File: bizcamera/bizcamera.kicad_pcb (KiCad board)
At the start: 4 copper layers, 84.5 x 55 mm, 81 parts, among them J1 Camera, J2 Micro_SD_Card_Det1, J3 USB_IN, SW1 USB_BOOT, SW3 Shutter, U1 RP2350_60QFN, U2 SPX3819M5-L-1-8, U3 S25FS128SDSNFI101, U4 ESP-PSRAM64, U5 SPX3819M5-L-3-3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

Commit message: Update bizcamera.kicad_pcb
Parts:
- moved R17 2.03 mm to (123.9, 67.9), turned to -90 degrees
- moved D1 1.89 mm to (125.5, 70.3)
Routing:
- net Net-(D1-A): track 74.2 -> 70.9 mm
- net /USB_DN: track 18.4 -> 19.4 mm
- net /USB_DP: track 20.2 -> 21.2 mm
- net -BATT: track 133.7 -> 133.5 mm, vias 23 -> 24
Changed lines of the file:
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@@
 	(footprint "LED_SMD:LED_1206_3216Metric_ReverseMount_Hole1.8x2.4mm"
 		(layer "F.Cu")
-		(at 125.42 68.46)
+		(at 125.46 70.35)
 		(descr "LED SMD 1206 (3216 Metric), reverse mount, square (rectangular) end terminal, IPC_7351 nominal, (Body size source: http://www.tortai-tech.com/upload/download/2011102023233369053.pdf), generated with kicad-footprint-generator")
 		(tags "diode reverse")
@@
 	(footprint "Resistor_SMD:R_0402_1005Metric"
 		(layer "F.Cu")
-		(at 123.45 65.91)
+		(at 123.92 67.88 -90)
 		(descr "Resistor SMD 0402 (1005 Metric), square (rectangular) end terminal, IPC_7351 nominal, (Body size source: IPC-SM-782 page 72, https://www.pcb-3d.com/wordpress/wp-content/uploads/ipc-sm-782a_amendment_1_and_2.pdf), generated with kicad-footprint-generator")
 		(tags "resistor")
 		(property "Reference" "R17"
-			(at 0 -1.17 0)
+			(at 0 -1.17 90)
 			(layer "F.SilkS")
 			(hide yes)
@@
 		)
 		(property "Value" "1k"
-			(at 0 1.17 0)
+			(at 0 1.17 90)
 			(layer "F.Fab")
 			(effects
@@
 		)
 		(property "Footprint" "Resistor_SMD:R_0402_1005Metric"
-			(at 0 0 0)
+			(at 0 0 -90)
 			(unlocked yes)
 			(layer "F.Fab")
@@
 		)
 		(property "Datasheet" ""
-			(at 0 0 0)
+			(at 0 0 -90)
 			(unlocked yes)
 			(layer "F.Fab")
@@
 		)
 		(property "Description" "Resistor"
-			(at 0 0 0)
+			(at 0 0 -90)
 			(unlocked yes)
 			(layer "F.Fab")
@@
 		(attr smd)
 		(fp_line
-			(start -0.153641 -0.38)
-			(end 0.153641 -0.38)
+			(start -0.153641 0.38)
+			(end 0.153641 0.38)
 			(stroke
 				(width 0.12)
@@
 		)
 		(fp_line
-			(start -0.153641 0.38)
-			(end 0.153641 0.38)
+			(start -0.153641 -0.38)
+			(end 0.153641 -0.38)
 			(stroke
 				(width 0.12)
@@
 		)
 		(fp_line
-			(start -0.93 -0.47)
-			(end 0.93 -0.47)
+			(start -0.93 0.47)
+			(end -0.93 -0.47)
 			(stroke
 				(width 0.05)
@@
 		)
 		(fp_line
-			(start -0.93 0.47)
-			(end -0.93 -0.47)
+			(start 0.93 0.47)
+			(end -0.93 0.47)
 			(stroke
 				(width 0.05)
@@
 		)
 		(fp_line
-			(start 0.93 -0.47)
-			(end 0.93 0.47)
+			(start -0.93 -0.47)
+			(end 0.93 -0.47)
 			(stroke
 				(width 0.05)
@@
 		)
 		(fp_line
-			(start 0.93 0.47)
-			(end -0.93 0.47)
+			(start 0.93 -0.47)
+			(end 0.93 0.47)
 			(stroke
 				(width 0.05)
@@
 		)
 		(fp_line
-			(start -0.525 -0.27)
-			(end 0.525 -0.27)
+			(start -0.525 0.27)
+			(end -0.525 -0.27)
 			(stroke
 				(width 0.1)
@@
 		)
 		(fp_line
-			(start -0.525 0.27)
-			(end -0.525 -0.27)
+			(start 0.525 0.27)
+			(end -0.525 0.27)
 			(stroke
 				(width 0.1)
@@
 		)
 		(fp_line
-			(start 0.525 -0.27)
-			(end 0.525 0.27)
+			(start -0.525 -0.27)
+			(end 0.525 -0.27)
 			(stroke
 				(width 0.1)
@@
 		)
 		(fp_line
-			(start 0.525 0.27)
-			(end -0.525 0.27)
+			(start 0.525 -0.27)
+			(end 0.525 0.27)
 			(stroke
 				(width 0.1)
@@
 		)
 		(fp_text user "${REFERENCE}"
-			(at 0 0 0)
+			(at 0 0 90)
 			(layer "F.Fab")
 			(effects
@@
 		)
 		(pad "1" smd roundrect
-			(at -0.51 0)
+			(at -0.51 0 270)
 			(size 0.54 0.64)
 			(layers "F.Cu" "F.Paste" "F.Mask")
@@
 		)
 		(pad "2" smd roundrect
-			(at 0.51 0)
+			(at 0.51 0 270)
 			(size 0.54 0.64)
 			(layers "F.Cu" "F.Paste" "F.Mask")
@@
 	)
 	(segment
-		(start 121.915 66.935)
-		(end 121.915 67.98)
-		(width 0.35)
-		(layer "F.Cu")
-		(net 2)
-	)
-	(segment
 		(start 177.857501 114.8925)
 		(end 176.6475 113.682499)
@@
 	)
 	(segment
+		(start 122.525 67.37)
+		(end 121.915 67.98)
+		(width 0.35)
+		(layer "F.Cu")
+		(net 2)
+	)
+	(segment
 		(start 181.050768 93.82)
 		(end 180.02625 93.82)
@@
 	)
 	(segment
-		(start 122.94 65.91)
-		(end 121.915 66.935)
-		(width 0.35)
-		(layer "F.Cu")
-		(net 2)
-	)
-	(segment
 		(start 112.49 92.25)
 		(end 116.78 92.25)
@@
 	)
 	(segment
+		(start 123.92 67.37)
+		(end 122.525 67.37)
+		(width 0.35)
+		(layer "F.Cu")
+		(net 2)
+	)
+	(segment
 		(start 187.72 85.68)
 		(end 187.69 85.65)
@@
 	)
 	(via
+		(at 148.19 113.7)
+		(size 0.5)
+		(drill 0.3)
+		(layers "F.Cu" "B.Cu")
+		(net 2)
+	)
+	(via
 		(at 172.3 107)
 		(size 0.6)
@@
 	)
 	(segment
-		(start 123.96 65.91)
-		(end 123.96 68.37)
+		(start 123.96 70.3)
+		(end 123.91 70.35)
 		(width 0.5)
 		(layer "F.Cu")
@@
 	)
 	(segment
+		(start 123.92 70.34)
+		(end 123.91 70.35)
+		(width 0.35)
+		(layer "F.Cu")
+		(net 47)
+	)
+	(segment
+		(start 123.92 68.39)
+		(end 123.92 70.34)
+		(width 0.35)
+		(layer "F.Cu")
+		(net 47)
+	)
+	(segment
 		(start 152.35 110.2)
 		(end 152.35 109.44)
@@
 	)
 	(segment
+		(start 178.9275 97.5325)
+		(end 178.9275 96.5125)
+		(width 0.2)
+		(layer "F.Cu")
+		(net 50)
+	)
+	(segment
 		(start 187.279999 89.25)
 		(end 188.255 89.25)
@@
 	)
 	(segment
-		(start 126.97 68.46)
-		(end 126.97 67.47)
-		(width 0.35)
-		(layer "F.Cu")
-		(net 64)
-	)
-	(segment
-		(start 126.97 67.47)
-		(end 126.6 67.1)
-		(width 0.35)
-		(layer "F.Cu")
-		(net 64)
-	)
-	(segment
 		(start 183.0975 105.5425)
 		(end 182.48624 105.5425)
@@
 	)
 	(via
-		(at 126.6 67.1)
+		(at 127.01 70.35)
 		(size 0.7)
 		(drill 0.4)
@@
 	)
 	(segment
-		(start 126.6 67.1)
-		(end 129.18 69.68)
-		(width 0.5)
-		(layer "In2.Cu")
-		(net 64)
-	)
-	(segment
-		(start 136.71206 69.68)
+		(start 137.38206 70.35)
 		(end 172.46206 105.43)
 		(width 0.5)
@@
 	)
 	(segment
-		(start 129.18 69.68)
-		(end 136.71206 69.68)
-		(width 0.5)
-		(layer "In2.Cu")
-		(net 64)
-	)
-	(segment
 		(start 182.19285 105.83589)
 		(end 181.78696 105.43)
@@
 	)
 	(segment
+		(start 127.01 70.35)
+		(end 137.38206 70.35)
+		(width 0.5)
+		(layer "In2.Cu")
+		(net 64)
+	)
+	(segment
 		(start 181.66 108.18)
 		(end 181.66 109.02)
@@
 		(width 0.2)
 		(layer "F.Cu")
+		(net 67)
+	)
+	(segment
+		(start 179.9175 97.5425)
+		(end 179.9175 96.5225)
+		(width 0.2)
+		(layer "F.Cu")

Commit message: Styling
Styling to make it more of a business card :D
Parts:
- removed kibuzzard-6824811E: G***, kibuzzard-6824811E
- removed kibuzzard-68248180: G***, kibuzzard-68248180
- added G***: LOGO, Kiyo:Blahaj Exposed copper, F.Cu at (134.3, 69.2)
- added REF**: KiCad-Logo2_5mm_Copper-exposed, Kiyo:KiCad-Logo2_5mm_Copper-exposed, F.Cu at (142.5, 72.4)
- added kibuzzard-68265B48: G***, kibuzzard-68265B48, B.Cu at (173.7, 72.0)
- added kibuzzard-68265CCE: G***, kibuzzard-68265CCE, B.Cu at (137.6, 72.5)
- added kibuzzard-68265CF0: G***, kibuzzard-68265CF0, B.Cu at (119.8, 70.3)
- added kibuzzard-68265EBA: G***, kibuzzard-68265EBA, F.Cu at (190.8, 103.6)
- added kibuzzard-68265EEF: G***, kibuzzard-68265EEF, F.Cu at (170.7, 77.1)
- added kibuzzard-68265F1C: G***, kibuzzard-68265F1C, F.Cu at (177.1, 76.6)
- added kibuzzard-68265F3A: G***, kibuzzard-68265F3A, F.Cu at (193.3, 98.4)
- added kibuzzard-68265F49: G***, kibuzzard-68265F49, F.Cu at (153.6, 93.0)
- added kibuzzard-68265FA3: G***, kibuzzard-68265FA3, F.Cu at (134.0, 113.4)
- added kibuzzard-68265FBA: G***, kibuzzard-68265FBA, F.Cu at (185.1, 85.2)
- added kibuzzard-68265FD3: G***, kibuzzard-68265FD3, F.Cu at (185.0, 89.0)
- added kibuzzard-68265FDC: G***, kibuzzard-68265FDC, F.Cu at (119.5, 113.4)
- added kibuzzard-68266036: G***, kibuzzard-68266036, F.Cu at (169.8, 106.7)
- moved C22 1.12 mm to (183.0, 87.3), turned to 90 degrees
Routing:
- net +5V: track 28.7 -> 21.6 mm
- net +3V3: track 34.9 -> 32.4 mm, vias 13 -> 12
- net /QSPI_SS: track 4.40 -> 6.17 mm
- net /SCLK: track 37.4 -> 39.2 mm
- net /SPI_DO: track 35.6 -> 37.4 mm
- net /SPI_CS: track 40.0 -> 41.7 mm
- net /SD_DET: track 36.7 -> 38.4 mm
- net /SPI_DI: track 39.5 -> 41.0 mm
- net +1V8: track 244.6 -> 243.4 mm, vias 11 -> 12
- net -BATT: track 133.5 -> 133.8 mm, vias 24 -> 27
- added copper zone on F.Cu, net +5V
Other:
- board text added: "Liam Brooks Photographer Hobby PCB Designer https://kiyoo.moe github: korewakiyo discord: korewakiyo"

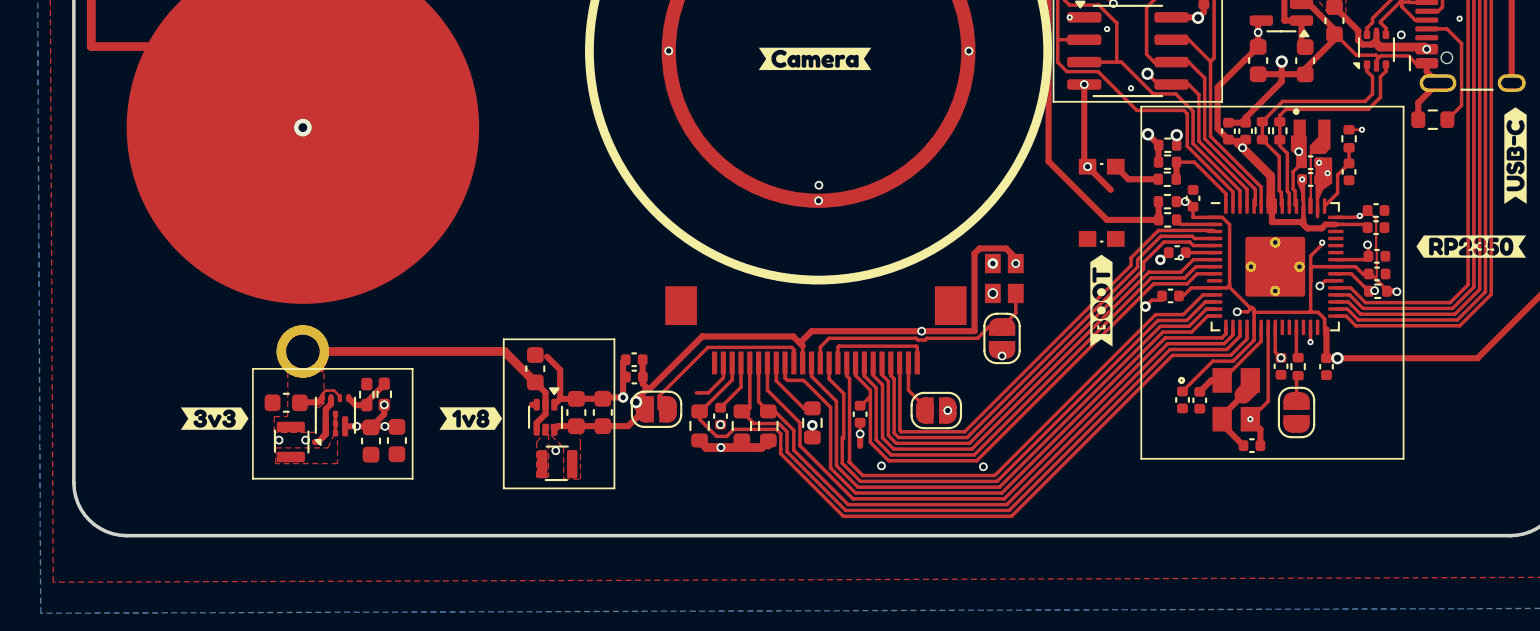
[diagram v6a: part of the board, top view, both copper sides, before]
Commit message: BOM and minor rework
I realised 68u 0603's were impossible lol
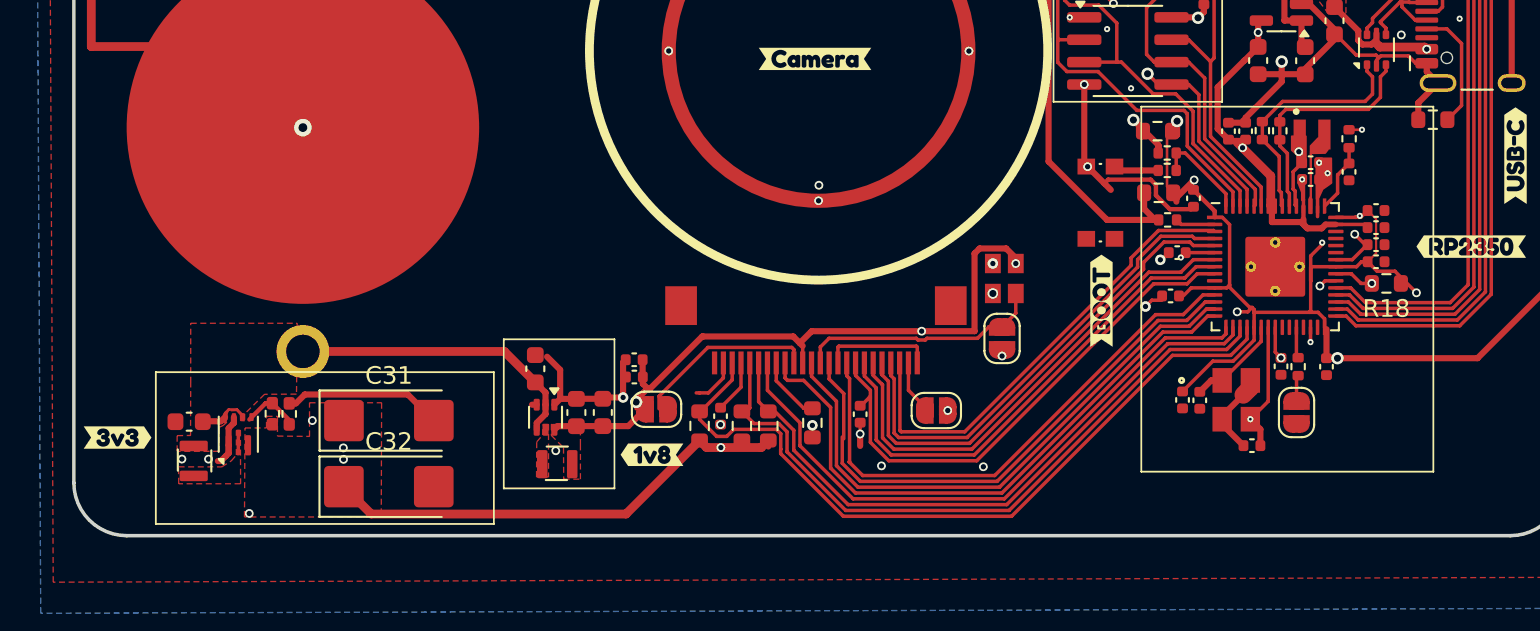
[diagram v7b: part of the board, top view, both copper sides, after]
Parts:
- removed kibuzzard-68265FA3: G***, kibuzzard-68265FA3
- added kibuzzard-682743A4: G***, kibuzzard-682743A4, F.Cu at (144.3, 115.4)
- C18: value 12p -> 15p
- C31, C32: footprint Capacitor_SMD:C_0603_1608Metric -> Capacitor_Tantalum_SMD:CP_EIA-6032-20_AVX-F_Pad2.25x2.35mm_HandSolder
- R10, R18, R7: footprint Resistor_SMD:R_0402_1005Metric -> Resistor_SMD:R_0603_1608Metric
- R13, R14, R15, R16: value 10K -> 10k
- moved R19 6.44 mm to (122.8, 113.1)
- moved U7 5.61 mm to (120.8, 114.2)
- moved L2 5.61 mm to (118.3, 115.7)
- moved C30 5.61 mm to (118.0, 113.5)
- moved kibuzzard-68265FDC 5.61 mm to (114.0, 114.4)
- moved R6 4.53 mm to (123.7, 113.1)
- moved C32 2.78 mm to (129.4, 117.2), turned to 0 degrees
- moved C31 1.22 mm to (129.4, 113.5), turned to 0 degrees
- moved R7 0.99 mm to (173.0, 97.0)
- moved R10 0.70 mm to (173.0, 100.5)
- moved C4 0.69 mm to (185.4, 104.5)
- moved C12 0.66 mm to (185.4, 103.5)
- moved R18 0.66 mm to (186.0, 105.7)
- moved R5 0.52 mm to (173.5, 98.3)
- moved R4 0.50 mm to (173.5, 99.3)
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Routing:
- net +3V3: track 32.4 -> 50.5 mm, vias 12 -> 13
- net -BATT: track 133.8 -> 149.1 mm
- net +1V8: track 243.4 -> 249.2 mm
- net +BATT: track 48.0 -> 46.5 mm
- net Net-(U4-~{CE}): track 20.0 -> 21.3 mm
- net +1V1: track 46.4 -> 47.4 mm
- net Net-(U1-GPIO25): track 89.1 -> 88.4 mm
- net /QSPI_SS: track 6.17 -> 5.47 mm
- added copper zone on F.Cu, net +3V3
